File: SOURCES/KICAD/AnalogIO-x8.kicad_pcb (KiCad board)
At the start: 2 copper layers, 120 x 120 mm, 418 parts, among them IC101 IC_TLE2426ID, IC102 IC_ADM811TARTZ, IC103 IC_LM1117MP-5.0, IC104 IC_LM1117MPX-ADJ, IC105 IC_NCP1117LPST33, IC201 IC_NE5532AD_SOIC8, IC202 IC_NE5532AD_SOIC8, IC203 IC_NE5532AD_SOIC8, IC204 IC_NE5532AD_SOIC8, IC205 IC_AK5558VN, IC206 IC_NE5532AD_SOIC8, IC207 IC_NE5532AD_SOIC8, IC208 IC_NE5532AD_SOIC8, IC209 IC_NE5532AD_SOIC8, IC301 IC_NE5532AD_SOIC8, IC302 IC_NE5532AD_SOIC8, IC303 IC_NE5532AD_SOIC8, IC304 IC_NE5532AD_SOIC8, IC305 IC_AK4458VN, IC306 IC_NE5532AD_SOIC8, IC307 IC_NE5532AD_SOIC8, IC308 IC_NE5532AD_SOIC8, IC309 IC_NE5532AD_SOIC8, X101 CON_IDC64, X102 CON_IDC64, X103 CON_MicroFit3_02x02, X104 CON_MicroFit3_02x02, X201 CON_IDC26, X202 CON_DSUB25F, X301 CON_DSUB25F, X302 CON_IDC26

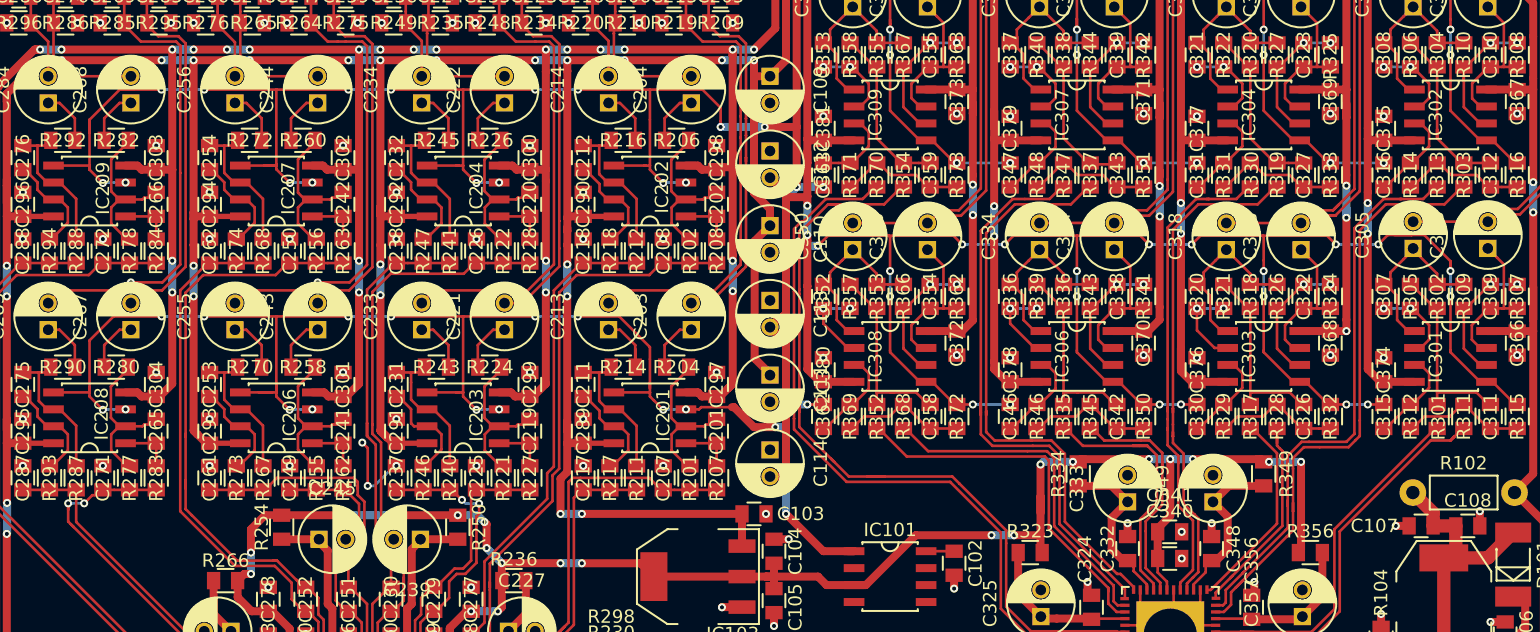
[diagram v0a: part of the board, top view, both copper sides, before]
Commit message: Convert to KiCad6 and clean up
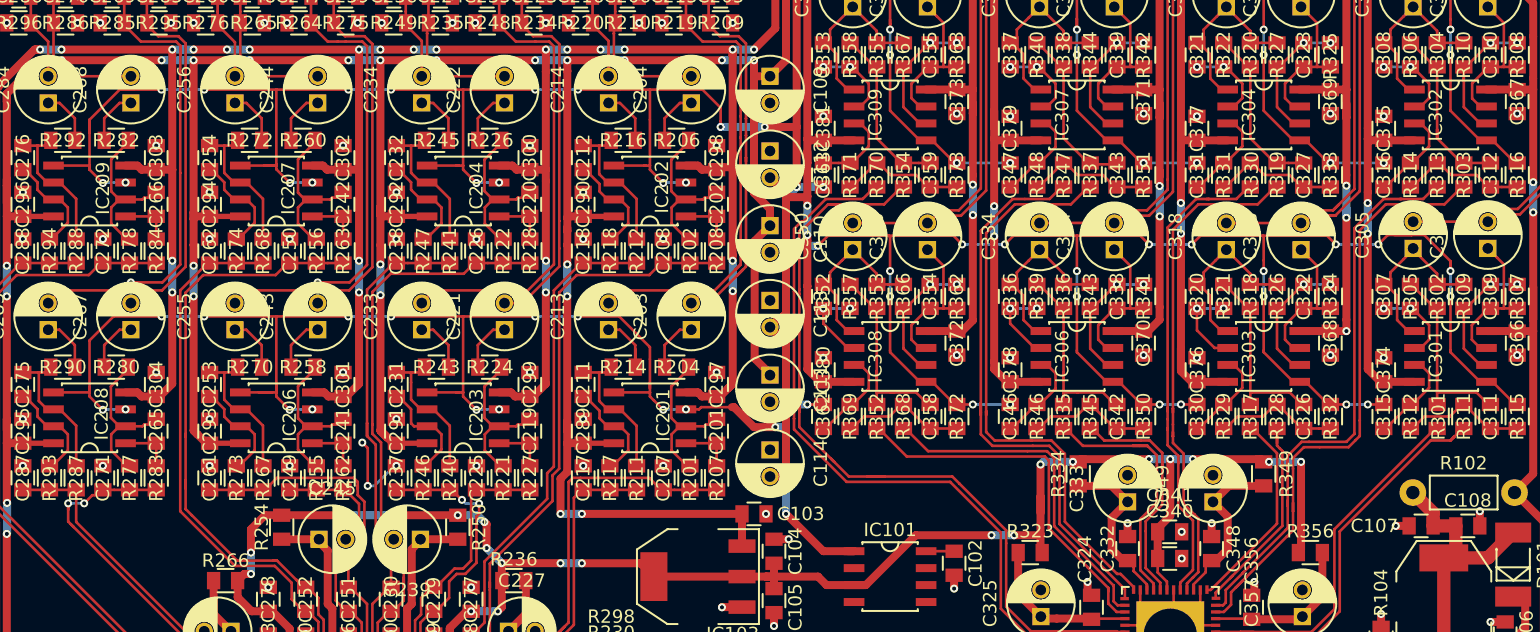
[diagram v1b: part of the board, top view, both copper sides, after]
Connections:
- net /~RST renamed /~{RST}
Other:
- net class Default removed

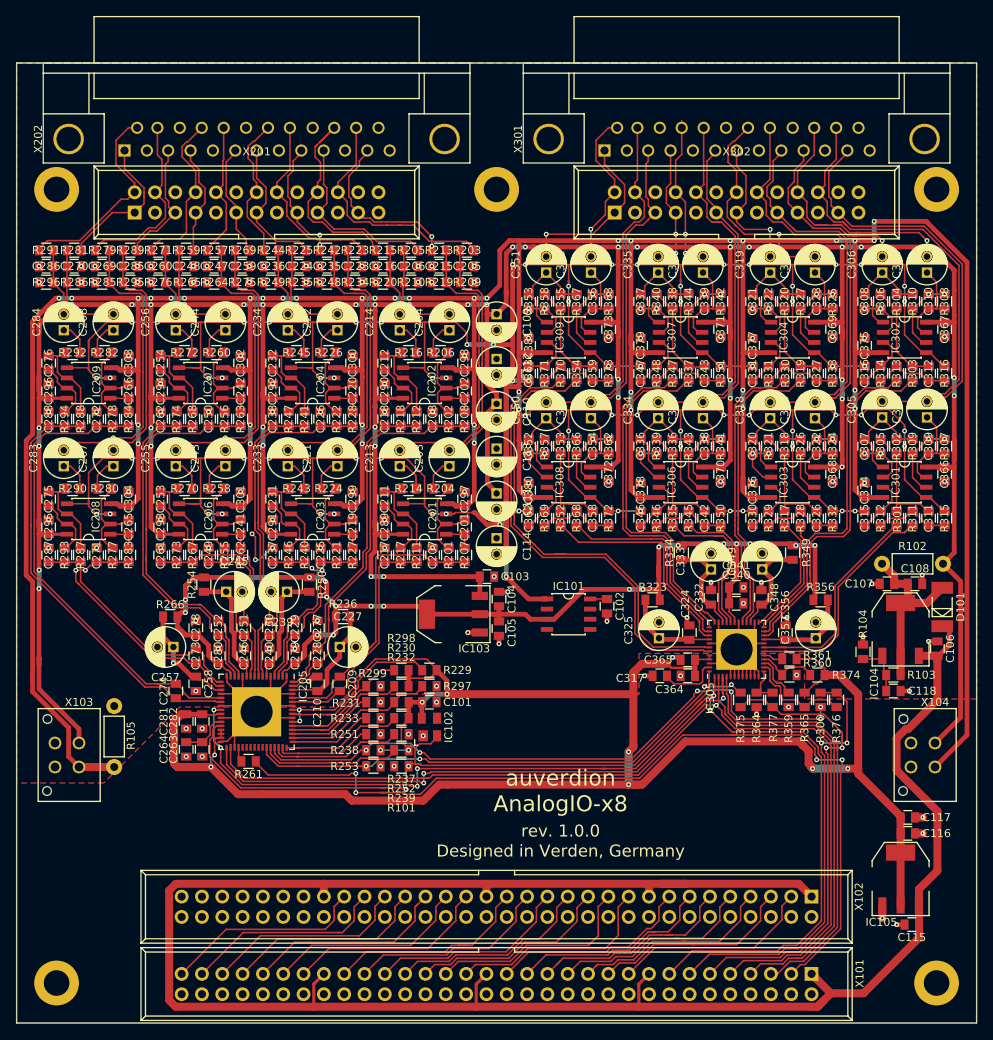
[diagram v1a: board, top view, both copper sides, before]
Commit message: Rescue footprints to local library
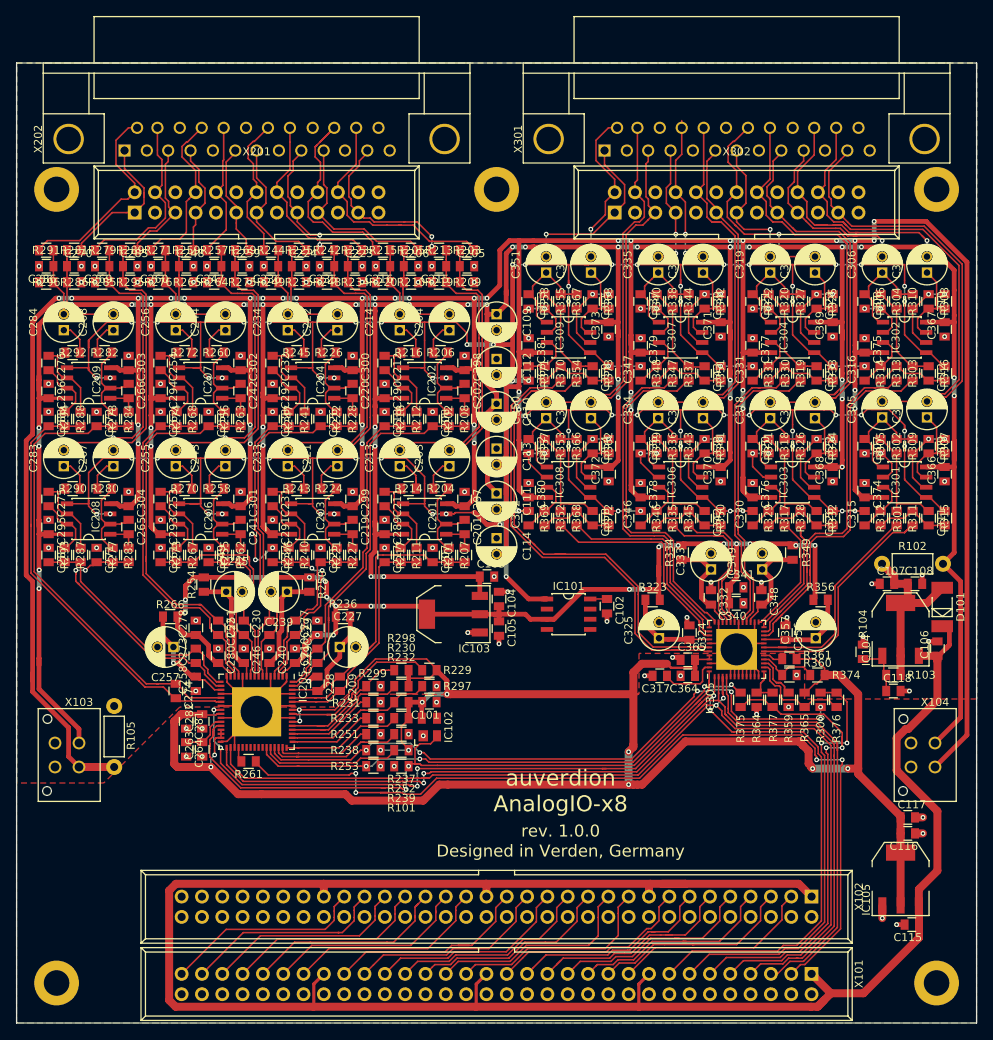
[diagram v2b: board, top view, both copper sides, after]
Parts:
- B101, B102, B103, B104, B105: footprint rklib:MountingHole_3.2mm_M3_DIN965_Pad -> AnalogIO-x8:MountingHole_3.2mm_M3_DIN965_Pad
- C101, C102, C103, C104, C105, C106, C107, C108, C115, C116, C117, C118, C201, C202, C205, C206, C207, C208, C209, C210, C211, C212, C215, C216, C217, C218, C219, C220, C223, C224, C225, C226, C228, C229, C230, C231, C232, C235, C236, C237, C238, C240, C241, C242, C246, C247, C248, C249, C250, C251, C252, C253, C254, C258, C259, C260, C261, C262, C263, C264, C265, C266, C269, C270, C271, C272, C273, C274, C275, C276, C277, C278, C279, C280, C281, C282, C285, C286, C287, C288, C289, C290, C291, C292, C293, C294, C295, C296, C297, C298, C299, C300, C301, C302, C303, C304, C307, C308, C309, C310, C311, C312, C315, C316, C317, C320, C321, C322, C323, C324, C326, C327, C330, C331, C332, C336, C337, C338, C339, C340, C341, C342, C343, C346, C347, C348, C352, C353, C354, C355, C356, C358, C359, C362, C363, C364, C365, C366, C367, C368, C369, C370, C371, C372, C373, C374, C375, C376, C377, C378, C379, C380, C381: footprint rklib:C0805-X7R -> AnalogIO-x8:C0805-X7R
- C109, C110, C111, C112, C113, C114, C203, C204, C213, C214, C221, C222, C227, C233, C234, C239, C243, C244, C245, C255, C256, C257, C267, C268, C283, C284, C305, C306, C313, C314, C318, C319, C325, C328, C329, C333, C334, C335, C344, C345, C349, C350, C351, C357, C360, C361: footprint rklib:RD2_D5_L11 -> AnalogIO-x8:RD2_D5_L11
- IC101: footprint rklib:SOIC8_3.9x4.9mm_Pitch1.27mm -> AnalogIO-x8:SOIC8_3.9x4.9mm_Pitch1.27mm
- IC103, IC104, IC105: footprint rklib:SOT223 -> AnalogIO-x8:SOT223
- X101, X102: footprint rklib:IDC64 -> AnalogIO-x8:IDC64
- X103, X104: footprint rklib:Microfit3_43045-0428 -> AnalogIO-x8:Microfit3_43045-0428
- X201, X302: footprint rklib:IDC26 -> AnalogIO-x8:IDC26
- X202, X301: footprint rklib:DSUB25FC -> AnalogIO-x8:DSUB25FC
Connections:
- net /ADC-1/ADC1+ renamed /ADC/ADC1+
- net /ADC-1/ADC1- renamed /ADC/ADC1-
- net /ADC-1/ADC2+ renamed /ADC/ADC2+
- net /ADC-1/ADC2- renamed /ADC/ADC2-
- net /ADC-1/ADC3+ renamed /ADC/ADC3+
- net /ADC-1/ADC3- renamed /ADC/ADC3-
- net /ADC-1/ADC4+ renamed /ADC/ADC4+
- net /ADC-1/ADC4- renamed /ADC/ADC4-
- net /ADC-1/ADC5+ renamed /ADC/ADC5+
- net /ADC-1/ADC5- renamed /ADC/ADC5-
- net /ADC-1/ADC6+ renamed /ADC/ADC6+
- net /ADC-1/ADC6- renamed /ADC/ADC6-
- net /ADC-1/ADC7+ renamed /ADC/ADC7+
- net /ADC-1/ADC7- renamed /ADC/ADC7-
- net /ADC-1/ADC8+ renamed /ADC/ADC8+
- net /ADC-1/ADC8- renamed /ADC/ADC8-
- net /ADC-1/AIN1+ renamed /ADC/AIN1+
- net /ADC-1/AIN1- renamed /ADC/AIN1-
- net /ADC-1/AIN2+ renamed /ADC/AIN2+
- net /ADC-1/AIN2- renamed /ADC/AIN2-
- net /ADC-1/AIN3+ renamed /ADC/AIN3+
- net /ADC-1/AIN3- renamed /ADC/AIN3-
- net /ADC-1/AIN4+ renamed /ADC/AIN4+
- net /ADC-1/AIN4- renamed /ADC/AIN4-
- net /ADC-1/AIN5+ renamed /ADC/AIN5+
- net /ADC-1/AIN5- renamed /ADC/AIN5-
- net /ADC-1/AIN6+ renamed /ADC/AIN6+
- net /ADC-1/AIN6- renamed /ADC/AIN6-
- net /ADC-1/AIN7+ renamed /ADC/AIN7+
- net /ADC-1/AIN7- renamed /ADC/AIN7-
- net /ADC-1/AIN8+ renamed /ADC/AIN8+
- net /ADC-1/AIN8- renamed /ADC/AIN8-
- net /ADC-1/IN1+ renamed /ADC/IN1+
- net /ADC-1/IN1- renamed /ADC/IN1-
- net /ADC-1/IN2+ renamed /ADC/IN2+
- net /ADC-1/IN2- renamed /ADC/IN2-
- net /ADC-1/IN3+ renamed /ADC/IN3+
- net /ADC-1/IN3- renamed /ADC/IN3-
- net /ADC-1/IN4+ renamed /ADC/IN4+
- net /ADC-1/IN4- renamed /ADC/IN4-
- net /ADC-1/IN5+ renamed /ADC/IN5+
- net /ADC-1/IN5- renamed /ADC/IN5-
- net /ADC-1/IN6+ renamed /ADC/IN6+
- net /ADC-1/IN6- renamed /ADC/IN6-
- net /ADC-1/IN7+ renamed /ADC/IN7+
- net /ADC-1/IN7- renamed /ADC/IN7-
- net /ADC-1/IN8+ renamed /ADC/IN8+
- net /ADC-1/IN8- renamed /ADC/IN8-
- net /DAC-1/AOUT1+ renamed /DAC/AOUT1+
- net /DAC-1/AOUT1- renamed /DAC/AOUT1-
- net /DAC-1/AOUT2+ renamed /DAC/AOUT2+
- net /DAC-1/AOUT2- renamed /DAC/AOUT2-
- net /DAC-1/AOUT3+ renamed /DAC/AOUT3+
- net /DAC-1/AOUT3- renamed /DAC/AOUT3-
- net /DAC-1/AOUT4+ renamed /DAC/AOUT4+
- net /DAC-1/AOUT4- renamed /DAC/AOUT4-
- net /DAC-1/AOUT5+ renamed /DAC/AOUT5+
- net /DAC-1/AOUT5- renamed /DAC/AOUT5-
- net /DAC-1/AOUT6+ renamed /DAC/AOUT6+
- net /DAC-1/AOUT6- renamed /DAC/AOUT6-
- net /DAC-1/AOUT7+ renamed /DAC/AOUT7+
- net /DAC-1/AOUT7- renamed /DAC/AOUT7-
- net /DAC-1/AOUT8+ renamed /DAC/AOUT8+
- net /DAC-1/AOUT8- renamed /DAC/AOUT8-
- net /DAC-1/DAC1+ renamed /DAC/DAC1+
- net /DAC-1/DAC1- renamed /DAC/DAC1-
- net /DAC-1/DAC2+ renamed /DAC/DAC2+
- net /DAC-1/DAC2- renamed /DAC/DAC2-
- net /DAC-1/DAC3+ renamed /DAC/DAC3+
- net /DAC-1/DAC3- renamed /DAC/DAC3-
- net /DAC-1/DAC4+ renamed /DAC/DAC4+
- net /DAC-1/DAC4- renamed /DAC/DAC4-
- net /DAC-1/DAC5+ renamed /DAC/DAC5+
- net /DAC-1/DAC5- renamed /DAC/DAC5-
- net /DAC-1/DAC6+ renamed /DAC/DAC6+
- net /DAC-1/DAC6- renamed /DAC/DAC6-
- net /DAC-1/DAC7+ renamed /DAC/DAC7+
- net /DAC-1/DAC7- renamed /DAC/DAC7-
- net /DAC-1/DAC8+ renamed /DAC/DAC8+
- net /DAC-1/DAC8- renamed /DAC/DAC8-
- B101 pad 1: (no net) -> unconnected-(B101-Pad1)
- B102 pad 1: (no net) -> unconnected-(B102-Pad1)
- B103 pad 1: (no net) -> unconnected-(B103-Pad1)
- B104 pad 1: (no net) -> unconnected-(B104-Pad1)
- B105 pad 1: (no net) -> unconnected-(B105-Pad1)
- IC102 pad 3: (no net) -> unconnected-(IC102-Pad3)
- IC205 pad 37: (no net) -> unconnected-(IC205-Pad37)
- IC205 pad 38: (no net) -> unconnected-(IC205-Pad38)
- IC205 pad 39: (no net) -> unconnected-(IC205-Pad39)
- IC205 pad 40: (no net) -> unconnected-(IC205-Pad40)
- IC205 pad 41: (no net) -> unconnected-(IC205-Pad41)
- IC205 pad 42: (no net) -> /ADC/OVF
- X102 pad 51: (no net) -> unconnected-(X102-Pad51)
- X102 pad 53: (no net) -> unconnected-(X102-Pad53)
- X102 pad 55: (no net) -> unconnected-(X102-Pad55)
- X102 pad 57: (no net) -> unconnected-(X102-Pad57)
- X102 pad 59: (no net) -> unconnected-(X102-Pad59)
- X102 pad 61: (no net) -> unconnected-(X102-Pad61)
- X102 pad 63: (no net) -> unconnected-(X102-Pad63)
- X201 pad 25: (no net) -> unconnected-(X201-Pad25)
- X201 pad 26: (no net) -> unconnected-(X201-Pad26)
- X202 pad 13: (no net) -> unconnected-(X202-Pad13)
- X301 pad 13: (no net) -> unconnected-(X301-Pad13)
- X302 pad 25: (no net) -> unconnected-(X302-Pad25)
- X302 pad 26: (no net) -> unconnected-(X302-Pad26)
